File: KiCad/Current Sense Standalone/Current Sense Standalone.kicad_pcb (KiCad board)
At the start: 2 copper layers, 62.3 x 24.3 mm, 9 parts, among them J1 PLUG INPUT BATTERY IN HERE (X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, J3 V+/- TEST Header PIN, J6 to MCU GPIO PIN, J7 PLUG BATTERY OUTPUT HERE (XT6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, U1 INA139QPWRQ1

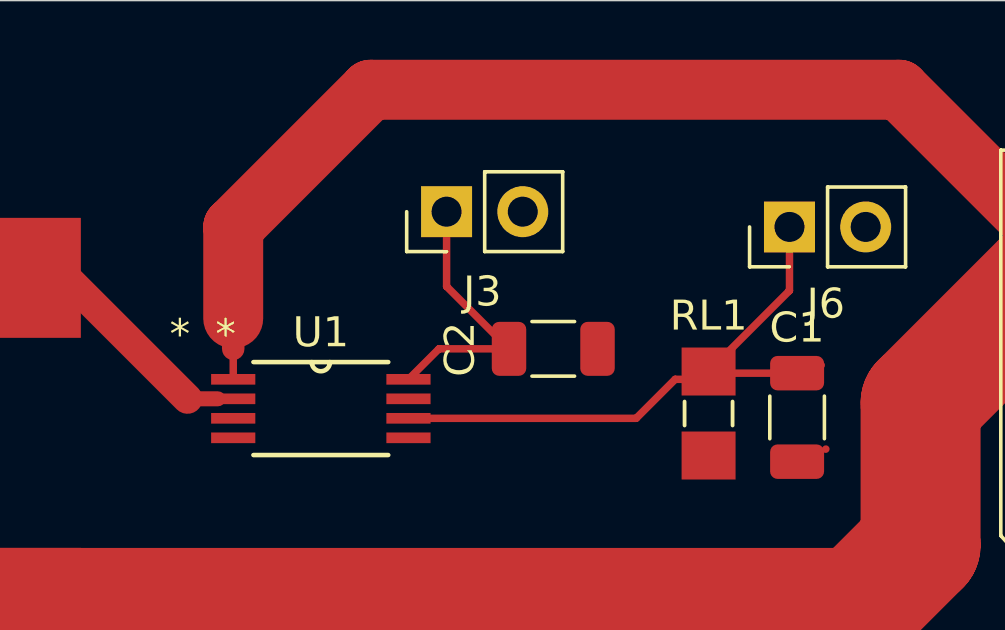
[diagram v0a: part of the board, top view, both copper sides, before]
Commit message: Fuse test circuit and updated current sense
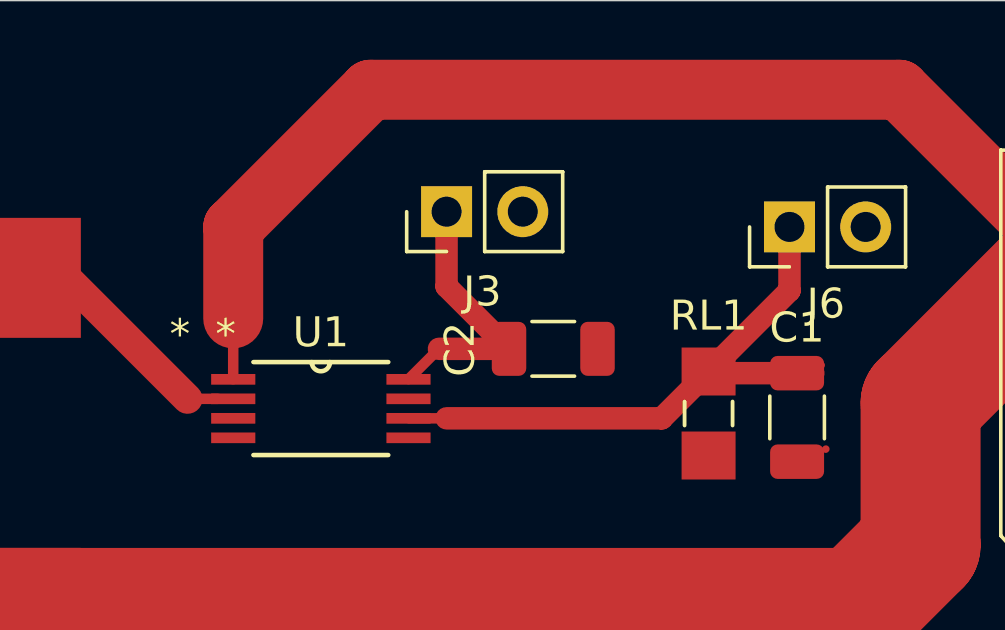
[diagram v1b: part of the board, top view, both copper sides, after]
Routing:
- net /Vout: track 20.6 -> 21.1 mm
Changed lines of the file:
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@@
   (gr_rect (start 12.606153 12.7) (end 74.93 37.026478)
     (stroke (width 0.2) (type default)) (fill none) (layer "Edge.Cuts"))
-  (segment (start 57.15 20.32) (end 57.15 22.443375) (width 0.25) (layer "F.Cu") (net 1))
-  (segment (start 57.15 22.443375) (end 54.663751 24.929624) (width 0.25) (layer "F.Cu") (net 1))
+  (segment (start 57.15 20.32) (end 57.15 22.443375) (width 0.75) (layer "F.Cu") (net 1))
+  (segment (start 57.15 22.443375) (end 54.663751 24.929624) (width 0.75) (layer "F.Cu") (net 1))
   (segment (start 54.663751 24.929624) (end 54.453375 24.929624) (width 0.25) (layer "F.Cu") (net 1))
   (segment (start 57.942862 25.195) (end 58.208238 24.929624) (width 0.25) (layer "F.Cu") (net 1))
-  (segment (start 53.34 25.4) (end 53.982999 25.4) (width 0.25) (layer "F.Cu") (net 1))
-  (segment (start 54.718751 25.195) (end 57.942862 25.195) (width 0.25) (layer "F.Cu") (net 1))
-  (segment (start 44.45 26.7) (end 52.04 26.7) (width 0.25) (layer "F.Cu") (net 1))
+  (segment (start 54.718751 25.195) (end 57.942862 25.195) (width 0.75) (layer "F.Cu") (net 1))
+  (segment (start 44.45 26.7) (end 45.72 26.7) (width 0.35) (layer "F.Cu") (net 1))
+  (segment (start 45.72 26.7) (end 52.893375 26.7) (width 0.75) (layer "F.Cu") (net 1))
+  (segment (start 52.893375 26.7) (end 54.453375 25.14) (width 0.75) (layer "F.Cu") (net 1))
   (segment (start 53.982999 25.4) (end 54.453375 24.929624) (width 0.25) (layer "F.Cu") (net 1))
   (segment (start 54.453375 24.929624) (end 54.718751 25.195) (width 0.25) (layer "F.Cu") (net 1))
-  (segment (start 52.04 26.7) (end 53.34 25.4) (width 0.25) (layer "F.Cu") (net 1))
   (segment (start 58.363078 27.724784) (end 58.358238 27.729624) (width 0.25) (layer "F.Cu") (net 2))
   (segment (start 18.650936 29.21) (end 20.510938 27.349998) (width 0.25) (layer "F.Cu") (net 2))
   (segment (start 54.663751 27.729624) (end 54.043375 28.35) (width 0.25) (layer "F.Cu") (net 2))
-  (segment (start 44.45 25.4) (end 45.466 24.384) (width 0.25) (layer "F.Cu") (net 3))
-  (segment (start 45.466 24.384) (end 47.801 24.384) (width 0.25) (layer "F.Cu") (net 3))
-  (segment (start 45.72 22.303) (end 45.72 19.812) (width 0.25) (layer "F.Cu") (net 3))
-  (segment (start 47.801 24.384) (end 45.72 22.303) (width 0.25) (layer "F.Cu") (net 3))
+  (segment (start 44.45 25.4) (end 45.466 24.384) (width 0.35) (layer "F.Cu") (net 3))
+  (segment (start 45.72 22.303) (end 45.72 19.812) (width 0.75) (layer "F.Cu") (net 3))
+  (segment (start 47.801 24.384) (end 45.72 22.303) (width 0.75) (layer "F.Cu") (net 3))
+  (segment (start 45.466 24.384) (end 47.801 24.384) (width 0.75) (layer "F.Cu") (net 3))
   (segment (start 18.650936 22.01) (end 29.621262 22.01) (width 4) (layer "F.Cu") (net 7))
   (segment (start 29.621262 22.01) (end 29.629273 22.018011) (width 4) (layer "F.Cu") (net 7))
+  (segment (start 38.1 26.049998) (end 38.608 26.049998) (width 0.25) (layer "F.Cu") (net 7))
   (segment (start 28.279273 23.368011) (end 29.629273 22.018011) (width 0.25) (layer "F.Cu") (net 7))
-  (segment (start 38.1 26.049998) (end 38.608 26.049998) (width 0.25) (layer "F.Cu") (net 7))
+  (segment (start 18.650936 22.01) (end 20.008947 23.368011) (width 0.25) (layer "F.Cu") (net 7))
+  (segment (start 37.084 26.049998) (end 38.1 26.049998) (width 0.35) (layer "F.Cu") (net 7))
+  (segment (start 37.084 26.049998) (end 33.052013 22.018011) (width 1) (layer "F.Cu") (net 7))
   (segment (start 33.052013 22.018011) (end 29.629273 22.018011) (width 1) (layer "F.Cu") (net 7))
-  (segment (start 37.084 26.049998) (end 38.1 26.049998) (width 0.5) (layer "F.Cu") (net 7))
-  (segment (start 18.650936 22.01) (end 20.008947 23.368011) (width 0.25) (layer "F.Cu") (net 7))
-  (segment (start 37.084 26.049998) (end 33.052013 22.018011) (width 1) (layer "F.Cu") (net 7))
   (segment (start 18.650936 20.130973) (end 18.650936 22.01) (width 0.25) (layer "F.Cu") (net 7))
   (segment (start 65.693027 22.01) (end 68.344045 22.01) (width 4) (layer "F.Cu") (net 8))
   (segment (start 61.52 26.183027) (end 65.693027 22.01) (width 4) (layer "F.Cu") (net 8))
+  (segment (start 38.608 20.32) (end 43.18 15.748) (width 2) (layer "F.Cu") (net 8))
+  (segment (start 60.812045 15.748) (end 67.074045 22.01) (width 2) (layer "F.Cu") (net 8))
+  (segment (start 38.608 23.368) (end 38.608 25.4) (width 0.35) (layer "F.Cu") (net 8))
+  (segment (start 29.629273 33.018011) (end 29.631262 33.02) (width 2) (layer "F.Cu") (net 8))
+  (segment (start 59.436 33.02) (end 61.52 30.936) (width 4) (layer "F.Cu") (net 8))
+  (segment (start 29.631262 33.02) (end 59.436 33.02) (width 4) (layer "F.Cu") (net 8))
   (segment (start 38.608 23.368) (end 38.608 20.32) (width 2) (layer "F.Cu") (net 8))
   (segment (start 43.18 15.748) (end 60.812045 15.748) (width 2) (layer "F.Cu") (net 8))
-  (segment (start 29.629273 33.018011) (end 29.631262 33.02) (width 2) (layer "F.Cu") (net 8))
-  (segment (start 38.608 20.32) (end 43.18 15.748) (width 2) (layer "F.Cu") (net 8))
-  (segment (start 59.436 33.02) (end 61.52 30.936) (width 4) (layer "F.Cu") (net 8))
-  (segment (start 29.631262 33.02) (end 59.436 33.02) (width 4) (layer "F.Cu") (net 8))
-  (segment (start 60.812045 15.748) (end 67.074045 22.01) (width 2) (layer "F.Cu") (net 8))
-  (segment (start 38.608 23.368) (end 38.608 24.384) (width 0.75) (layer "F.Cu") (net 8))
-  (segment (start 38.608 24.384) (end 38.608 25.4) (width 0.25) (layer "F.Cu") (net 8))
   (segment (start 61.52 30.936) (end 61.52 26.183027) (width 4) (layer "F.Cu") (net 8))
   (zone (net 2) (net_name "GND") (layers "F&B.Cu") (hatch edge 0.5)

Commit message: rearranged schematic for current sense
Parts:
- J7: value PLUG BATTERY OUTPUT HERE (XT60) -> PLUG OUTPUT CONNECTION HERE (XT60)
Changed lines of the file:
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@@
   (net 5 "unconnected-(U1-NC-Pad5)")
   (net 6 "unconnected-(U1-NC-Pad7)")
-  (net 7 "/Batt+")
-  (net 8 "/Batt-")
+  (net 7 "/Batt-")
+  (net 8 "/Batt+")
   (footprint "Mechatronic Footprints:AMASS_XT60-F_1x02_P7.20mm_Vertical" (layer "F.Cu")
     (at 68.344045 29.21 90)
@@
         (effects (font (size 1 1) (thickness 0.15)))
     )
-    (fp_text value "PLUG BATTERY OUTPUT HERE (XT60)" (at -0.042893 -6.908027 90) (layer "F.Fab") hide
+    (fp_text value "PLUG OUTPUT CONNECTION HERE (XT60)" (at -0.042893 -6.908027 90) (layer "F.Fab") hide
         (effects (font (size 1 1) (thickness 0.15)))
     )
@@
       (net 2 "GND") (pinfunction "Pin_1") (pintype "passive"))
     (pad "2" thru_hole circle (at 7.2 0 90) (size 6 6) (drill 4.5) (layers "*.Cu" "*.Mask")
-      (net 8 "/Batt-") (pinfunction "Pin_2") (pintype "passive"))
+      (net 7 "/Batt-") (pinfunction "Pin_2") (pintype "passive"))
     (model "${KISYS3DMOD}/Connector_AMASS.3dshapes/AMASS_XT60-F_1x02_P7.2mm_Vertical.wrl"
       (offset (xyz 0 0 0))
@@
     )
     (pad "1" smd rect (at -5.5 0 180) (size 7.8 4) (layers "F.Cu" "F.Paste" "F.Mask")
-      (net 8 "/Batt-") (pintype "passive") (thermal_bridge_angle 45))
+      (net 7 "/Batt-") (pintype "passive") (thermal_bridge_angle 45))
     (pad "2" smd rect (at 5.5 0 180) (size 7.8 4) (layers "F.Cu" "F.Paste" "F.Mask")
-      (net 7 "/Batt+") (pintype "passive") (thermal_bridge_angle 45))
+      (net 8 "/Batt+") (pintype "passive") (thermal_bridge_angle 45))
   )
   (footprint "Capacitor_SMD:C_1206_3216Metric" (layer "F.Cu")
@@
       (stroke (width 0.0254) (type solid)) (layer "F.Fab"))
     (pad "1" smd rect (at -2.921 -0.974999) (size 1.4732 0.3556) (layers "F.Cu" "F.Paste" "F.Mask")
-      (net 8 "/Batt-") (pinfunction "VIN-") (pintype "input"))
+      (net 7 "/Batt-") (pinfunction "VIN-") (pintype "input"))
     (pad "2" smd rect (at -2.921 -0.325001) (size 1.4732 0.3556) (layers "F.Cu" "F.Paste" "F.Mask")
-      (net 7 "/Batt+") (pinfunction "VIN+") (pintype "input"))
+      (net 8 "/Batt+") (pinfunction "VIN+") (pintype "input"))
     (pad "3" smd rect (at -2.921 0.325001) (size 1.4732 0.3556) (layers "F.Cu" "F.Paste" "F.Mask")
       (net 4 "unconnected-(U1-NC-Pad3)") (pinfunction "NC") (pintype "unspecified+no_connect"))
@@
       (net 2 "GND") (pinfunction "Pin_1") (pintype "passive"))
     (pad "2" thru_hole circle (at 7.2 0 90) (size 6 6) (drill 4.5) (layers "*.Cu" "*.Mask")
-      (net 7 "/Batt+") (pinfunction "Pin_2") (pintype "passive"))
+      (net 8 "/Batt+") (pinfunction "Pin_2") (pintype "passive"))
     (model "${KISYS3DMOD}/Connector_AMASS.3dshapes/AMASS_XT60-M_1x02_P7.2mm_Vertical.wrl"
       (offset (xyz 0 0 0))
@@
   (segment (start 47.801 24.384) (end 45.72 22.303) (width 0.75) (layer "F.Cu") (net 3))
   (segment (start 45.466 24.384) (end 47.801 24.384) (width 0.75) (layer "F.Cu") (net 3))
-  (segment (start 18.650936 22.01) (end 29.621262 22.01) (width 4) (layer "F.Cu") (net 7))
-  (segment (start 29.621262 22.01) (end 29.629273 22.018011) (width 4) (layer "F.Cu") (net 7))
-  (segment (start 38.1 26.049998) (end 38.608 26.049998) (width 0.25) (layer "F.Cu") (net 7))
-  (segment (start 28.279273 23.368011) (end 29.629273 22.018011) (width 0.25) (layer "F.Cu") (net 7))
-  (segment (start 18.650936 22.01) (end 20.008947 23.368011) (width 0.25) (layer "F.Cu") (net 7))
-  (segment (start 37.084 26.049998) (end 38.1 26.049998) (width 0.35) (layer "F.Cu") (net 7))
-  (segment (start 37.084 26.049998) (end 33.052013 22.018011) (width 1) (layer "F.Cu") (net 7))
-  (segment (start 33.052013 22.018011) (end 29.629273 22.018011) (width 1) (layer "F.Cu") (net 7))
-  (segment (start 18.650936 20.130973) (end 18.650936 22.01) (width 0.25) (layer "F.Cu") (net 7))
-  (segment (start 65.693027 22.01) (end 68.344045 22.01) (width 4) (layer "F.Cu") (net 8))
-  (segment (start 61.52 26.183027) (end 65.693027 22.01) (width 4) (layer "F.Cu") (net 8))
-  (segment (start 38.608 20.32) (end 43.18 15.748) (width 2) (layer "F.Cu") (net 8))
-  (segment (start 60.812045 15.748) (end 67.074045 22.01) (width 2) (layer "F.Cu") (net 8))
-  (segment (start 38.608 23.368) (end 38.608 25.4) (width 0.35) (layer "F.Cu") (net 8))
-  (segment (start 29.629273 33.018011) (end 29.631262 33.02) (width 2) (layer "F.Cu") (net 8))
-  (segment (start 59.436 33.02) (end 61.52 30.936) (width 4) (layer "F.Cu") (net 8))
-  (segment (start 29.631262 33.02) (end 59.436 33.02) (width 4) (layer "F.Cu") (net 8))
-  (segment (start 38.608 23.368) (end 38.608 20.32) (width 2) (layer "F.Cu") (net 8))
-  (segment (start 43.18 15.748) (end 60.812045 15.748) (width 2) (layer "F.Cu") (net 8))
-  (segment (start 61.52 30.936) (end 61.52 26.183027) (width 4) (layer "F.Cu") (net 8))
+  (segment (start 65.693027 22.01) (end 68.344045 22.01) (width 4) (layer "F.Cu") (net 7))
+  (segment (start 61.52 26.183027) (end 65.693027 22.01) (width 4) (layer "F.Cu") (net 7))
+  (segment (start 38.608 20.32) (end 43.18 15.748) (width 2) (layer "F.Cu") (net 7))
+  (segment (start 60.812045 15.748) (end 67.074045 22.01) (width 2) (layer "F.Cu") (net 7))
+  (segment (start 38.608 23.368) (end 38.608 25.4) (width 0.35) (layer "F.Cu") (net 7))
+  (segment (start 29.629273 33.018011) (end 29.631262 33.02) (width 2) (layer "F.Cu") (net 7))
+  (segment (start 59.436 33.02) (end 61.52 30.936) (width 4) (layer "F.Cu") (net 7))
+  (segment (start 29.631262 33.02) (end 59.436 33.02) (width 4) (layer "F.Cu") (net 7))
+  (segment (start 38.608 23.368) (end 38.608 20.32) (width 2) (layer "F.Cu") (net 7))
+  (segment (start 43.18 15.748) (end 60.812045 15.748) (width 2) (layer "F.Cu") (net 7))
+  (segment (start 61.52 30.936) (end 61.52 26.183027) (width 4) (layer "F.Cu") (net 7))
+  (segment (start 18.650936 22.01) (end 29.621262 22.01) (width 4) (layer "F.Cu") (net 8))
+  (segment (start 29.621262 22.01) (end 29.629273 22.018011) (width 4) (layer "F.Cu") (net 8))
+  (segment (start 38.1 26.049998) (end 38.608 26.049998) (width 0.25) (layer "F.Cu") (net 8))
+  (segment (start 28.279273 23.368011) (end 29.629273 22.018011) (width 0.25) (layer "F.Cu") (net 8))
+  (segment (start 18.650936 22.01) (end 20.008947 23.368011) (width 0.25) (layer "F.Cu") (net 8))
+  (segment (start 37.084 26.049998) (end 38.1 26.049998) (width 0.35) (layer "F.Cu") (net 8))
+  (segment (start 37.084 26.049998) (end 33.052013 22.018011) (width 1) (layer "F.Cu") (net 8))
+  (segment (start 33.052013 22.018011) (end 29.629273 22.018011) (width 1) (layer "F.Cu") (net 8))
+  (segment (start 18.650936 20.130973) (end 18.650936 22.01) (width 0.25) (layer "F.Cu") (net 8))
   (zone (net 2) (net_name "GND") (layers "F&B.Cu") (hatch edge 0.5)
     (connect_pads yes (clearance 0.5))
